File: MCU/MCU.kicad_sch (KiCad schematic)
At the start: 5 parts, among them J2 Conn_01x02, J3 Conn_01x02, J4 Conn_01x02, J5 Conn_01x02, U1 Nucleo_L432KC

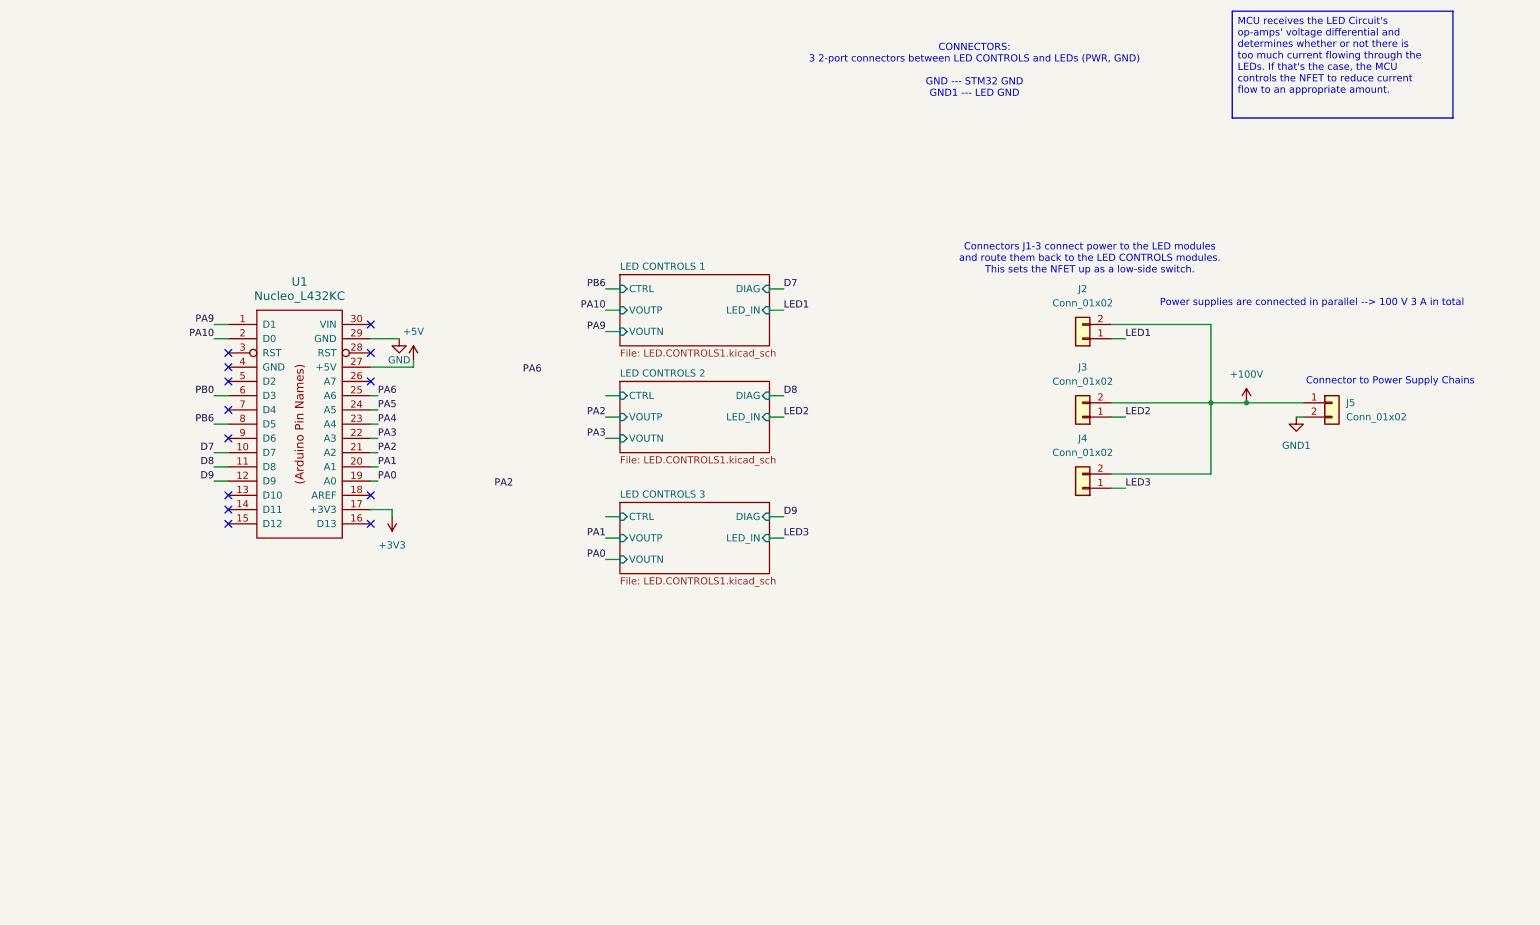
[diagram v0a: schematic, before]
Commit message: almost done with MCU: need to change TP names, adjust RTD on MCU
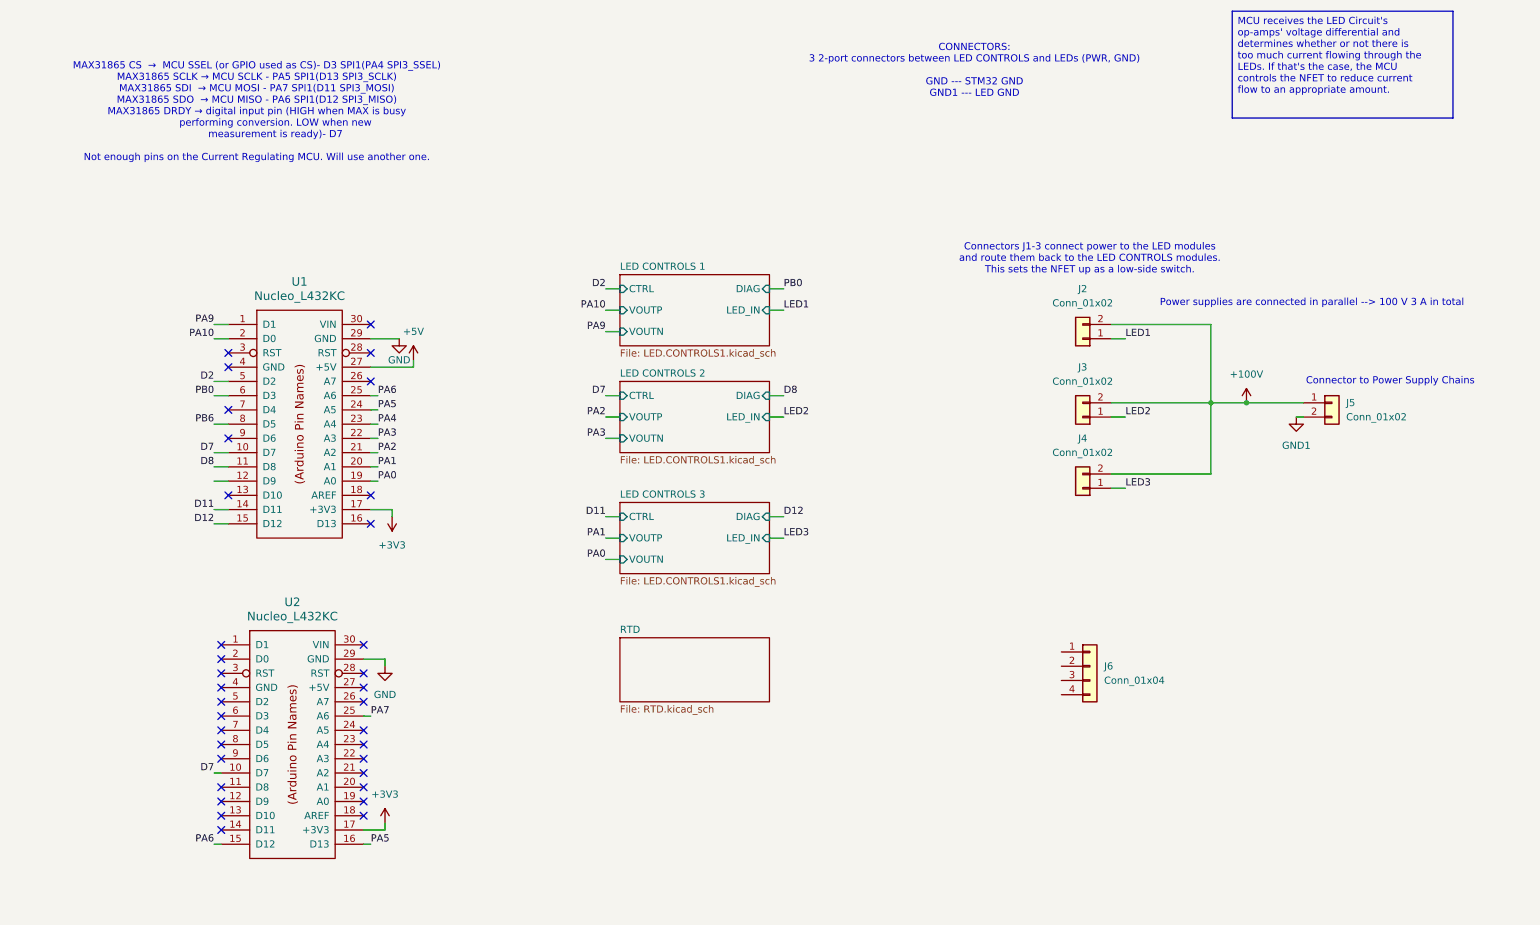
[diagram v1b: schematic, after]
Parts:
- added J6: Conn_01x04, Connector_JST:JST_EH_B4B-EH-A_1x04_P2.50mm_Vertical, symbol Connector_Generic:Conn_01x04
- added U2: Nucleo_L432KC, UTSVT STM32:NucleoL432KC, symbol nucleo_stm32:Nucleo_L432KC
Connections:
- net +3V3: now also U2.17 (+3V3)
- net D7: now also U2.10 (D7)
- net GND: now also U2.29 (GND)
- net PA5: now also U2.16 (D13)
- net PA6: now also U2.15 (D12)
- net D11: now reaches U1.14 (D11)
- net D12: now reaches U1.15 (D12)
- net D2: now reaches U1.5 (D2)
- net D9: no longer names the net of U1.12 (D9)
- new net PA7: U2.25 (A6)
- no-connect marks 13 -> 34
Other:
- added sheet RTD (RTD.kicad_sch)
- note added: "MAX31865 CS → MCU SSEL (or GPIO used as CS)- D3 SPI1(PA4 SPI3_SSEL) MAX31865 SCLK → MCU SCLK - PA5 SPI1(D13 SPI3_SCLK) MAX31865 SDI → MCU MOSI - PA7 SPI1(D11 SPI3_MOSI) MAX31865 SDO → MCU MISO - PA6 SPI1(D12 SPI3_MISO) MAX31865 DRDY → digital input pin (HIGH when MAX is busy performing conversion. LOW when new measurement is ready)- D7 Not enough pins on the Current Regulating MCU. Will use anoth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"

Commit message: final?
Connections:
- net RTD/FORCE+: now reaches J6.1 (Pin_1)
- net RTD/RTDIN+: now reaches J6.2 (Pin_2)
- net RTD/FORCE-: now reaches J6.3 (Pin_3)
- net RTD/RTDIN-: now reaches J6.4 (Pin_4)
- net D9: now reaches U1.12 (D9)
- net D10: now reaches U1.13 (D10)
- net D13: now reaches U1.16 (D13)
- net D4: now reaches U1.7 (D4)
- net D6: now reaches U1.9 (D6)
- no-connect marks 34 -> 30
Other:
- sheet RTD ports: added CS, DRDY, FORCE+, FORCE-, RTDIN+, RTDIN-, SCLK, SDI, SDO; removed none
- note added: "Goes into RTD"
- moved on the sheet: J6

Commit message: silkscreen, edge cuts, other stuff fixes
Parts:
- added H1, H2, H3, H4: MountingHole_Pad, MountingHole:MountingHole_3.2mm_M3_Pad_TopBottom, symbol Mechanical:MountingHole_Pad
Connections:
- no-connect marks 30 -> 34
